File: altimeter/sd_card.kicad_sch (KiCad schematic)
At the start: 7 parts, among them J6 Micro_SD_Card

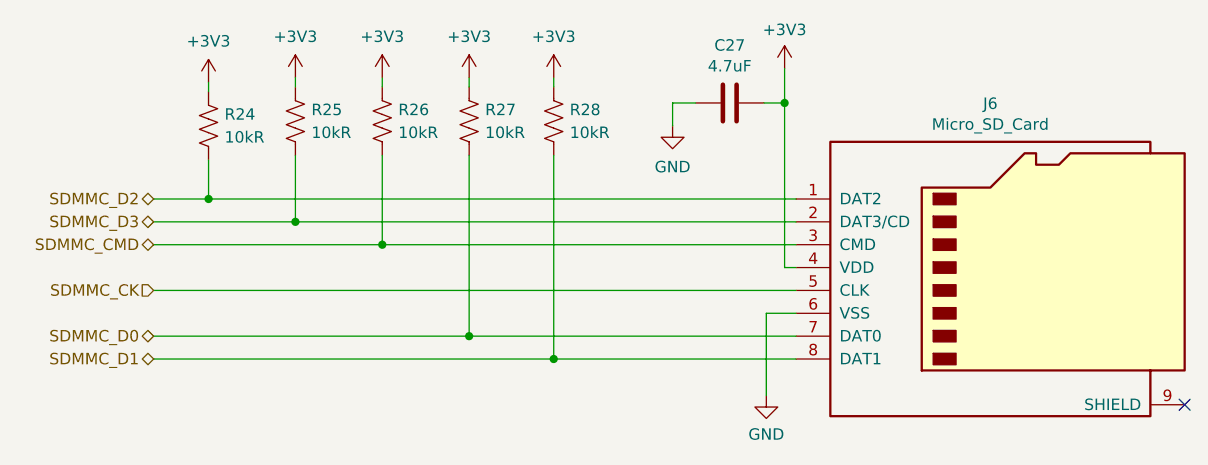
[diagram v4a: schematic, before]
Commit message: add adc filtering, remove capacitor on 3V3 buck output, update GPS connector
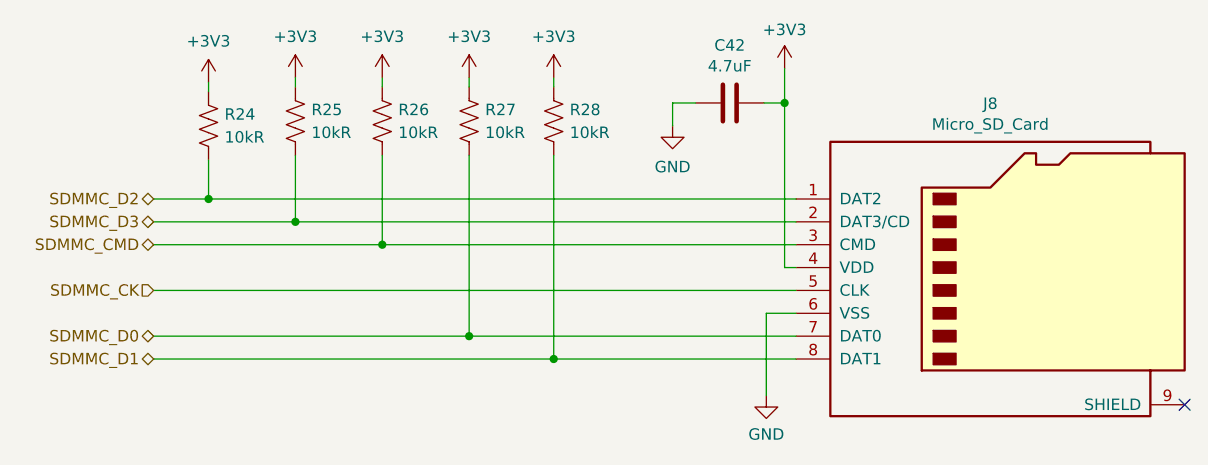
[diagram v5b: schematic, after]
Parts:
- renumbered C27 to C42, J6 to J8
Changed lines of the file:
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@@
 		(dnp no)
 		(fields_autoplaced yes)
-		(property "Reference" "#PWR064"
+		(property "Reference" "#PWR080"
 			(at 114.808 86.868 0)
 			(effects
@@
 			(project "altimeter"
 				(path "/d279ec14-0cf9-4295-bb74-26f70799167d/bb0bce4a-66e8-4d50-ad75-3628c6e07bf2/e008a181-ebf7-4a64-a582-05387fd5f501"
-					(reference "#PWR064")
+					(reference "#PWR080")
 					(unit 1)
 				)
@@
 		(dnp no)
 		(fields_autoplaced yes)
-		(property "Reference" "#PWR066"
+		(property "Reference" "#PWR082"
 			(at 134.112 86.868 0)
 			(effects
@@
 			(project "altimeter"
 				(path "/d279ec14-0cf9-4295-bb74-26f70799167d/bb0bce4a-66e8-4d50-ad75-3628c6e07bf2/e008a181-ebf7-4a64-a582-05387fd5f501"
-					(reference "#PWR066")
+					(reference "#PWR082")
 					(unit 1)
 				)
@@
 		(dnp no)
 		(fields_autoplaced yes)
-		(property "Reference" "#PWR065"
+		(property "Reference" "#PWR081"
 			(at 124.46 86.868 0)
 			(effects
@@
 			(project "altimeter"
 				(path "/d279ec14-0cf9-4295-bb74-26f70799167d/bb0bce4a-66e8-4d50-ad75-3628c6e07bf2/e008a181-ebf7-4a64-a582-05387fd5f501"
-					(reference "#PWR065")
+					(reference "#PWR081")
 					(unit 1)
 				)
@@
 		(dnp no)
 		(fields_autoplaced yes)
-		(property "Reference" "#PWR067"
+		(property "Reference" "#PWR083"
 			(at 143.51 86.868 0)
 			(effects
@@
 			(project "altimeter"
 				(path "/d279ec14-0cf9-4295-bb74-26f70799167d/bb0bce4a-66e8-4d50-ad75-3628c6e07bf2/e008a181-ebf7-4a64-a582-05387fd5f501"
-					(reference "#PWR067")
+					(reference "#PWR083")
 					(unit 1)
 				)
@@
 		(on_board yes)
 		(dnp no)
-		(property "Reference" "C27"
+		(property "Reference" "C42"
 			(at 163.068 79.4512 90)
 			(effects
@@
 			(project "altimeter"
 				(path "/d279ec14-0cf9-4295-bb74-26f70799167d/bb0bce4a-66e8-4d50-ad75-3628c6e07bf2/e008a181-ebf7-4a64-a582-05387fd5f501"
-					(reference "C27")
+					(reference "C42")
 					(unit 1)
 				)
@@
 		(dnp no)
 		(fields_autoplaced yes)
-		(property "Reference" "#PWR063"
+		(property "Reference" "#PWR079"
 			(at 105.156 87.376 0)
 			(effects
@@
 			(project "altimeter"
 				(path "/d279ec14-0cf9-4295-bb74-26f70799167d/bb0bce4a-66e8-4d50-ad75-3628c6e07bf2/e008a181-ebf7-4a64-a582-05387fd5f501"
-					(reference "#PWR063")
+					(reference "#PWR079")
 					(unit 1)
 				)
@@
 		(dnp no)
 		(fields_autoplaced yes)
-		(property "Reference" "#PWR069"
+		(property "Reference" "#PWR085"
 			(at 167.132 124.714 0)
 			(effects
@@
 			(project "altimeter"
 				(path "/d279ec14-0cf9-4295-bb74-26f70799167d/bb0bce4a-66e8-4d50-ad75-3628c6e07bf2/e008a181-ebf7-4a64-a582-05387fd5f501"
-					(reference "#PWR069")
+					(reference "#PWR085")
 					(unit 1)
 				)
@@
 		(dnp no)
 		(fields_autoplaced yes)
-		(property "Reference" "#PWR070"
+		(property "Reference" "#PWR086"
 			(at 169.164 85.852 0)
 			(effects
@@
 			(project "altimeter"
 				(path "/d279ec14-0cf9-4295-bb74-26f70799167d/bb0bce4a-66e8-4d50-ad75-3628c6e07bf2/e008a181-ebf7-4a64-a582-05387fd5f501"
-					(reference "#PWR070")
+					(reference "#PWR086")
 					(unit 1)
 				)
@@
 		(on_board yes)
 		(dnp no)
-		(property "Reference" "J6"
+		(property "Reference" "J8"
 			(at 192.024 85.9282 0)
 			(effects
@@
 			(project "altimeter"
 				(path "/d279ec14-0cf9-4295-bb74-26f70799167d/bb0bce4a-66e8-4d50-ad75-3628c6e07bf2/e008a181-ebf7-4a64-a582-05387fd5f501"
-					(reference "J6")
+					(reference "J8")
 					(unit 1)
 				)
@@
 		(dnp no)
 		(fields_autoplaced yes)
-		(property "Reference" "#PWR068"
+		(property "Reference" "#PWR084"
 			(at 156.718 94.742 0)
 			(effects
@@
 			(project "altimeter"
 				(path "/d279ec14-0cf9-4295-bb74-26f70799167d/bb0bce4a-66e8-4d50-ad75-3628c6e07bf2/e008a181-ebf7-4a64-a582-05387fd5f501"
-					(reference "#PWR068")
-					(unit 1)
-				)
+					(reference "#PWR084")
+					(unit 1)
+				)

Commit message: regen pdf, double check mosfet arming circuit, move buzzer from mosfet arming to mag switch arming, add text notes
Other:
- company: (none) -> Waterloo Rocketry
- title: (none) -> SRAD Altimeter
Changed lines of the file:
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@@
 	(generator_version "8.0")
 	(paper "A4")
+	(title_block
+		(title "SRAD Altimeter")
+		(date "2025-02-20")
+		(company "Waterloo Rocketry")
+		(comment 1 "Designer: Ash Lang")
+	)
 	(junction
 		(at 143.51 114.3)

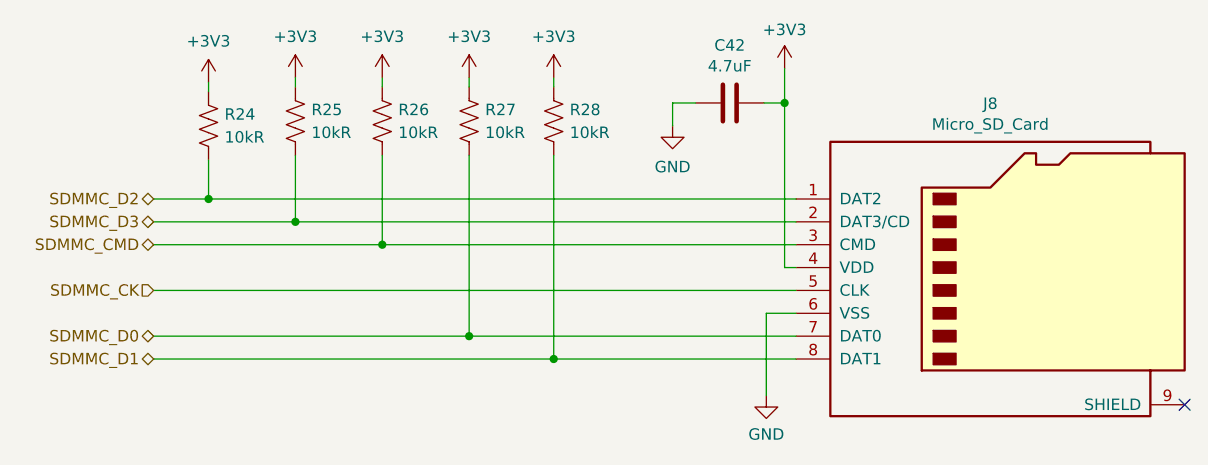
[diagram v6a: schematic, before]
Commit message: layout progress, swap buck converter for SOT23-6 package buck
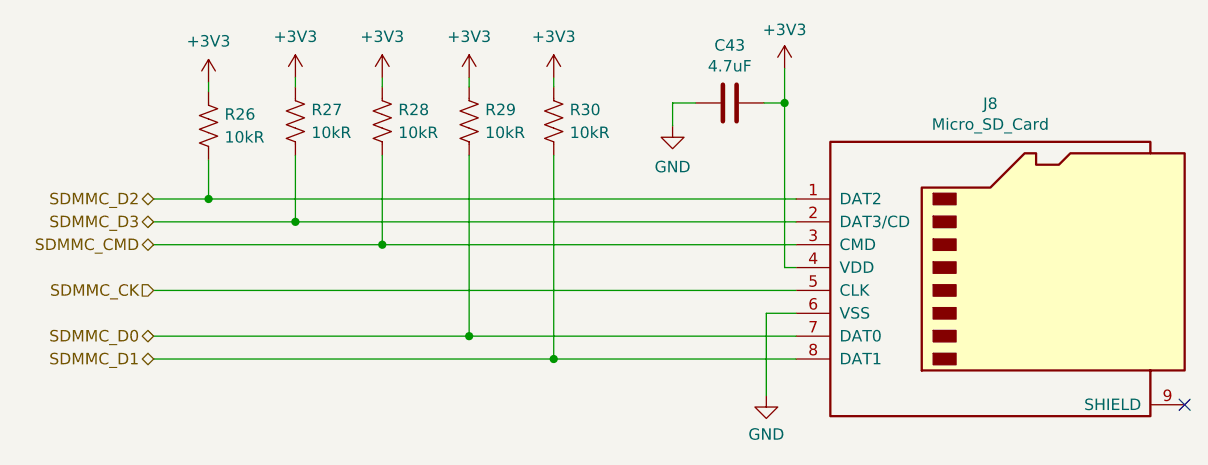
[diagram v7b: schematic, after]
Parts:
- renumbered C42 to C43, R24 to R26, R25 to R27, R26 to R28, R27 to R29, R28 to R30
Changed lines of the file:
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@@
 		(dnp no)
 		(fields_autoplaced yes)
-		(property "Reference" "R26"
+		(property "Reference" "R28"
 			(at 126.238 86.614 0)
 			(effects
@@
 			(project "altimeter"
 				(path "/d279ec14-0cf9-4295-bb74-26f70799167d/bb0bce4a-66e8-4d50-ad75-3628c6e07bf2/e008a181-ebf7-4a64-a582-05387fd5f501"
-					(reference "R26")
+					(reference "R28")
 					(unit 1)
 				)
@@
 		(dnp no)
 		(fields_autoplaced yes)
-		(property "Reference" "#PWR080"
+		(property "Reference" "#PWR085"
 			(at 114.808 86.868 0)
 			(effects
@@
 			(project "altimeter"
 				(path "/d279ec14-0cf9-4295-bb74-26f70799167d/bb0bce4a-66e8-4d50-ad75-3628c6e07bf2/e008a181-ebf7-4a64-a582-05387fd5f501"
-					(reference "#PWR080")
+					(reference "#PWR085")
 					(unit 1)
 				)
@@
 		(dnp no)
 		(fields_autoplaced yes)
-		(property "Reference" "#PWR082"
+		(property "Reference" "#PWR087"
 			(at 134.112 86.868 0)
 			(effects
@@
 			(project "altimeter"
 				(path "/d279ec14-0cf9-4295-bb74-26f70799167d/bb0bce4a-66e8-4d50-ad75-3628c6e07bf2/e008a181-ebf7-4a64-a582-05387fd5f501"
-					(reference "#PWR082")
+					(reference "#PWR087")
 					(unit 1)
 				)
@@
 		(dnp no)
 		(fields_autoplaced yes)
-		(property "Reference" "#PWR081"
+		(property "Reference" "#PWR086"
 			(at 124.46 86.868 0)
 			(effects
@@
 			(project "altimeter"
 				(path "/d279ec14-0cf9-4295-bb74-26f70799167d/bb0bce4a-66e8-4d50-ad75-3628c6e07bf2/e008a181-ebf7-4a64-a582-05387fd5f501"
-					(reference "#PWR081")
+					(reference "#PWR086")
 					(unit 1)
 				)
@@
 		(dnp no)
 		(fields_autoplaced yes)
-		(property "Reference" "#PWR083"
+		(property "Reference" "#PWR088"
 			(at 143.51 86.868 0)
 			(effects
@@
 			(project "altimeter"
 				(path "/d279ec14-0cf9-4295-bb74-26f70799167d/bb0bce4a-66e8-4d50-ad75-3628c6e07bf2/e008a181-ebf7-4a64-a582-05387fd5f501"
-					(reference "#PWR083")
+					(reference "#PWR088")
 					(unit 1)
 				)
@@
 		(dnp no)
 		(fields_autoplaced yes)
-		(property "Reference" "R28"
+		(property "Reference" "R30"
 			(at 145.288 86.614 0)
 			(effects
@@
 			(project "altimeter"
 				(path "/d279ec14-0cf9-4295-bb74-26f70799167d/bb0bce4a-66e8-4d50-ad75-3628c6e07bf2/e008a181-ebf7-4a64-a582-05387fd5f501"
-					(reference "R28")
+					(reference "R30")
 					(unit 1)
 				)
@@
 		(on_board yes)
 		(dnp no)
-		(property "Reference" "C42"
+		(property "Reference" "C43"
 			(at 163.068 79.4512 90)
 			(effects
@@
 			(project "altimeter"
 				(path "/d279ec14-0cf9-4295-bb74-26f70799167d/bb0bce4a-66e8-4d50-ad75-3628c6e07bf2/e008a181-ebf7-4a64-a582-05387fd5f501"
-					(reference "C42")
+					(reference "C43")
 					(unit 1)
 				)
@@
 		(dnp no)
 		(fields_autoplaced yes)
-		(property "Reference" "#PWR079"
+		(property "Reference" "#PWR084"
 			(at 105.156 87.376 0)
 			(effects
@@
 			(project "altimeter"
 				(path "/d279ec14-0cf9-4295-bb74-26f70799167d/bb0bce4a-66e8-4d50-ad75-3628c6e07bf2/e008a181-ebf7-4a64-a582-05387fd5f501"
-					(reference "#PWR079")
+					(reference "#PWR084")
 					(unit 1)
 				)
@@
 		(dnp no)
 		(fields_autoplaced yes)
-		(property "Reference" "R24"
+		(property "Reference" "R26"
 			(at 106.934 87.122 0)
 			(effects
@@
 			(project "altimeter"
 				(path "/d279ec14-0cf9-4295-bb74-26f70799167d/bb0bce4a-66e8-4d50-ad75-3628c6e07bf2/e008a181-ebf7-4a64-a582-05387fd5f501"
-					(reference "R24")
+					(reference "R26")
 					(unit 1)
 				)
@@
 		(dnp no)
 		(fields_autoplaced yes)
-		(property "Reference" "R25"
+		(property "Reference" "R27"
 			(at 116.586 86.614 0)
 			(effects
@@
 			(project "altimeter"
 				(path "/d279ec14-0cf9-4295-bb74-26f70799167d/bb0bce4a-66e8-4d50-ad75-3628c6e07bf2/e008a181-ebf7-4a64-a582-05387fd5f501"
-					(reference "R25")
+					(reference "R27")
 					(unit 1)
 				)
@@
 		(dnp no)
 		(fields_autoplaced yes)
-		(property "Reference" "#PWR085"
+		(property "Reference" "#PWR090"
 			(at 167.132 124.714 0)
 			(effects
@@
 			(project "altimeter"
 				(path "/d279ec14-0cf9-4295-bb74-26f70799167d/bb0bce4a-66e8-4d50-ad75-3628c6e07bf2/e008a181-ebf7-4a64-a582-05387fd5f501"
-					(reference "#PWR085")
+					(reference "#PWR090")
 					(unit 1)
 				)
@@
 		(dnp no)
 		(fields_autoplaced yes)
-		(property "Reference" "#PWR086"
+		(property "Reference" "#PWR091"
 			(at 169.164 85.852 0)
 			(effects
@@
 			(project "altimeter"
 				(path "/d279ec14-0cf9-4295-bb74-26f70799167d/bb0bce4a-66e8-4d50-ad75-3628c6e07bf2/e008a181-ebf7-4a64-a582-05387fd5f501"
-					(reference "#PWR086")
+					(reference "#PWR091")
 					(unit 1)
 				)
@@
 		(dnp no)
 		(fields_autoplaced yes)
-		(property "Reference" "R27"
+		(property "Reference" "R29"
 			(at 135.89 86.614 0)
 			(effects
@@
 			(project "altimeter"
 				(path "/d279ec14-0cf9-4295-bb74-26f70799167d/bb0bce4a-66e8-4d50-ad75-3628c6e07bf2/e008a181-ebf7-4a64-a582-05387fd5f501"
-					(reference "R27")
+					(reference "R29")
 					(unit 1)
 				)
@@
 		(dnp no)
 		(fields_autoplaced yes)
-		(property "Reference" "#PWR084"
+		(property "Reference" "#PWR089"
 			(at 156.718 94.742 0)
 			(effects
@@
 			(project "altimeter"
 				(path "/d279ec14-0cf9-4295-bb74-26f70799167d/bb0bce4a-66e8-4d50-ad75-3628c6e07bf2/e008a181-ebf7-4a64-a582-05387fd5f501"
-					(reference "#PWR084")
-					(unit 1)
-				)
+					(reference "#PWR089")
+					(unit 1)
+				)

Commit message: address Jack feedback
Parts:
- renumbered C43 to C40, J8 to J7, R26 to R32, R27 to R33, R28 to R34, R29 to R35, R30 to R36
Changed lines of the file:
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@@
 		(dnp no)
 		(fields_autoplaced yes)
-		(property "Reference" "R28"
+		(property "Reference" "R34"
 			(at 126.238 86.614 0)
 			(effects
@@
 			(project "altimeter"
 				(path "/d279ec14-0cf9-4295-bb74-26f70799167d/bb0bce4a-66e8-4d50-ad75-3628c6e07bf2/e008a181-ebf7-4a64-a582-05387fd5f501"
-					(reference "R28")
+					(reference "R34")
 					(unit 1)
 				)
@@
 		(dnp no)
 		(fields_autoplaced yes)
-		(property "Reference" "#PWR085"
+		(property "Reference" "#PWR078"
 			(at 114.808 86.868 0)
 			(effects
@@
 			(project "altimeter"
 				(path "/d279ec14-0cf9-4295-bb74-26f70799167d/bb0bce4a-66e8-4d50-ad75-3628c6e07bf2/e008a181-ebf7-4a64-a582-05387fd5f501"
-					(reference "#PWR085")
+					(reference "#PWR078")
 					(unit 1)
 				)
@@
 		(dnp no)
 		(fields_autoplaced yes)
-		(property "Reference" "#PWR087"
+		(property "Reference" "#PWR080"
 			(at 134.112 86.868 0)
 			(effects
@@
 			(project "altimeter"
 				(path "/d279ec14-0cf9-4295-bb74-26f70799167d/bb0bce4a-66e8-4d50-ad75-3628c6e07bf2/e008a181-ebf7-4a64-a582-05387fd5f501"
-					(reference "#PWR087")
+					(reference "#PWR080")
 					(unit 1)
 				)
@@
 		(dnp no)
 		(fields_autoplaced yes)
-		(property "Reference" "#PWR086"
+		(property "Reference" "#PWR079"
 			(at 124.46 86.868 0)
 			(effects
@@
 			(project "altimeter"
 				(path "/d279ec14-0cf9-4295-bb74-26f70799167d/bb0bce4a-66e8-4d50-ad75-3628c6e07bf2/e008a181-ebf7-4a64-a582-05387fd5f501"
-					(reference "#PWR086")
+					(reference "#PWR079")
 					(unit 1)
 				)
@@
 		(dnp no)
 		(fields_autoplaced yes)
-		(property "Reference" "#PWR088"
+		(property "Reference" "#PWR081"
 			(at 143.51 86.868 0)
 			(effects
@@
 			(project "altimeter"
 				(path "/d279ec14-0cf9-4295-bb74-26f70799167d/bb0bce4a-66e8-4d50-ad75-3628c6e07bf2/e008a181-ebf7-4a64-a582-05387fd5f501"
-					(reference "#PWR088")
+					(reference "#PWR081")
 					(unit 1)
 				)
@@
 		(dnp no)
 		(fields_autoplaced yes)
-		(property "Reference" "R30"
+		(property "Reference" "R36"
 			(at 145.288 86.614 0)
 			(effects
@@
 			(project "altimeter"
 				(path "/d279ec14-0cf9-4295-bb74-26f70799167d/bb0bce4a-66e8-4d50-ad75-3628c6e07bf2/e008a181-ebf7-4a64-a582-05387fd5f501"
-					(reference "R30")
+					(reference "R36")
 					(unit 1)
 				)
@@
 		(on_board yes)
 		(dnp no)
-		(property "Reference" "C43"
+		(property "Reference" "C40"
 			(at 163.068 79.4512 90)
 			(effects
@@
 			(project "altimeter"
 				(path "/d279ec14-0cf9-4295-bb74-26f70799167d/bb0bce4a-66e8-4d50-ad75-3628c6e07bf2/e008a181-ebf7-4a64-a582-05387fd5f501"
-					(reference "C43")
+					(reference "C40")
 					(unit 1)
 				)
@@
 		(dnp no)
 		(fields_autoplaced yes)
-		(property "Reference" "#PWR084"
+		(property "Reference" "#PWR077"
 			(at 105.156 87.376 0)
 			(effects
@@
 			(project "altimeter"
 				(path "/d279ec14-0cf9-4295-bb74-26f70799167d/bb0bce4a-66e8-4d50-ad75-3628c6e07bf2/e008a181-ebf7-4a64-a582-05387fd5f501"
-					(reference "#PWR084")
+					(reference "#PWR077")
 					(unit 1)
 				)
@@
 		(dnp no)
 		(fields_autoplaced yes)
-		(property "Reference" "R26"
+		(property "Reference" "R32"
 			(at 106.934 87.122 0)
 			(effects
@@
 			(project "altimeter"
 				(path "/d279ec14-0cf9-4295-bb74-26f70799167d/bb0bce4a-66e8-4d50-ad75-3628c6e07bf2/e008a181-ebf7-4a64-a582-05387fd5f501"
-					(reference "R26")
+					(reference "R32")
 					(unit 1)
 				)
@@
 		(dnp no)
 		(fields_autoplaced yes)
-		(property "Reference" "R27"
+		(property "Reference" "R33"
 			(at 116.586 86.614 0)
 			(effects
@@
 			(project "altimeter"
 				(path "/d279ec14-0cf9-4295-bb74-26f70799167d/bb0bce4a-66e8-4d50-ad75-3628c6e07bf2/e008a181-ebf7-4a64-a582-05387fd5f501"
-					(reference "R27")
+					(reference "R33")
 					(unit 1)
 				)
@@
 		(dnp no)
 		(fields_autoplaced yes)
-		(property "Reference" "#PWR090"
+		(property "Reference" "#PWR083"
 			(at 167.132 124.714 0)
 			(effects
@@
 			(project "altimeter"
 				(path "/d279ec14-0cf9-4295-bb74-26f70799167d/bb0bce4a-66e8-4d50-ad75-3628c6e07bf2/e008a181-ebf7-4a64-a582-05387fd5f501"
-					(reference "#PWR090")
+					(reference "#PWR083")
 					(unit 1)
 				)
@@
 		(dnp no)
 		(fields_autoplaced yes)
-		(property "Reference" "#PWR091"
+		(property "Reference" "#PWR084"
 			(at 169.164 85.852 0)
 			(effects
@@
 			(project "altimeter"
 				(path "/d279ec14-0cf9-4295-bb74-26f70799167d/bb0bce4a-66e8-4d50-ad75-3628c6e07bf2/e008a181-ebf7-4a64-a582-05387fd5f501"
-					(reference "#PWR091")
+					(reference "#PWR084")
 					(unit 1)
 				)
@@
 		(dnp no)
 		(fields_autoplaced yes)
-		(property "Reference" "R29"
+		(property "Reference" "R35"
 			(at 135.89 86.614 0)
 			(effects
@@
 			(project "altimeter"
 				(path "/d279ec14-0cf9-4295-bb74-26f70799167d/bb0bce4a-66e8-4d50-ad75-3628c6e07bf2/e008a181-ebf7-4a64-a582-05387fd5f501"
-					(reference "R29")
+					(reference "R35")
 					(unit 1)
 				)
@@
 		(on_board yes)
 		(dnp no)
-		(property "Reference" "J8"
+		(property "Reference" "J7"
 			(at 192.024 85.9282 0)
 			(effects
@@
 			(project "altimeter"
 				(path "/d279ec14-0cf9-4295-bb74-26f70799167d/bb0bce4a-66e8-4d50-ad75-3628c6e07bf2/e008a181-ebf7-4a64-a582-05387fd5f501"
-					(reference "J8")
+					(reference "J7")
 					(unit 1)
 				)
@@
 		(dnp no)
 		(fields_autoplaced yes)
-		(property "Reference" "#PWR089"
+		(property "Reference" "#PWR082"
 			(at 156.718 94.742 0)
 			(effects
@@
 			(project "altimeter"
 				(path "/d279ec14-0cf9-4295-bb74-26f70799167d/bb0bce4a-66e8-4d50-ad75-3628c6e07bf2/e008a181-ebf7-4a64-a582-05387fd5f501"
-					(reference "#PWR089")
-					(unit 1)
-				)
+					(reference "#PWR082")
+					(unit 1)
+				)
